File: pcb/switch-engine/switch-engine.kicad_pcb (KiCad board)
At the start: 10 copper layers, 124 x 112 mm, 368 parts, among them J1 CONN_PCIE_PWR_8PIN, J10 CORTEX_DEBUG_ETM, J11 SMPM, J12 CONN_01X03, J13 PMOD_HOST, J14 ARF6-08-S-D-A-K-TR, J15 ARF6-08-S-D-A-K-TR, J16 CONN_01X10, J17 ARF6-08-S-D-A-K-TR, J18 ARF6-08-S-D-A-K-TR, J19 CONN_01X10, J2 CONN_IBC_MGMT, J20 0826-1G1T-23-F, J21 ARF6-08-S-D-A-K-TR, J22 ARF6-08-S-D-A-K-TR, J23 CONN_01X10, J24 SMPM, J26 RJ45, J3 CONN_01X03, J4 CORTEX_DEBUG_ETM, J5 FAN_01, J6 FAN_01, J7 JUMPER_0402, J8 XILINX_JTAG, J9 PMOD_HOST, M1 SCREWHOLE, M2 SCREWHOLE, M3 SCREWHOLE, M4 SCREWHOLE, M5 LOGO, M6 LOGO, M7 LOGO, M8 960-27-23-D-AB-0, Q2 SSM6N58NU, SW1 SWITCH, SW2 SWITCH, U1 STM32L431-QFN48, U10 74LVC1T45, U11 74LVC1T45, U12 74LVC1T45, U13 MT25QU256ABA8E12-0AUT, U14 ECS-1612MV-250-CN, U15 SIT9121AI-2BF-XXS156.250000G, U17 AT24MAC402, U18 74LVC1T45, U19 74LVC1T45, U2 MYMGK1R812ERSR, U20 74LVC1T45, U21 74LVC1T45, U22 ECS-1612MV-250-CN, U23 KSZ9031RN, U24 ESD224DQAR, U25 SIT9121AI-2BF-XXS156.250000G, U26 ESD224DQAR, U27 SIT9121AI-2BF-XXS156.250000G, U28 ADP1740ACPZ-2.5-R7, U29 ADM3101E_QFN, U3 MYMGK1R812ERSR, U4 MYMGK00506ERSR, U5 MYMGK00504ERSR, U6 MYMGK00504ERSR, U7 ADP1740ACPZ-1.8-R7, U8 XCKU5P-2FFVB676I, U9 STM32H735-UFBGA176-25

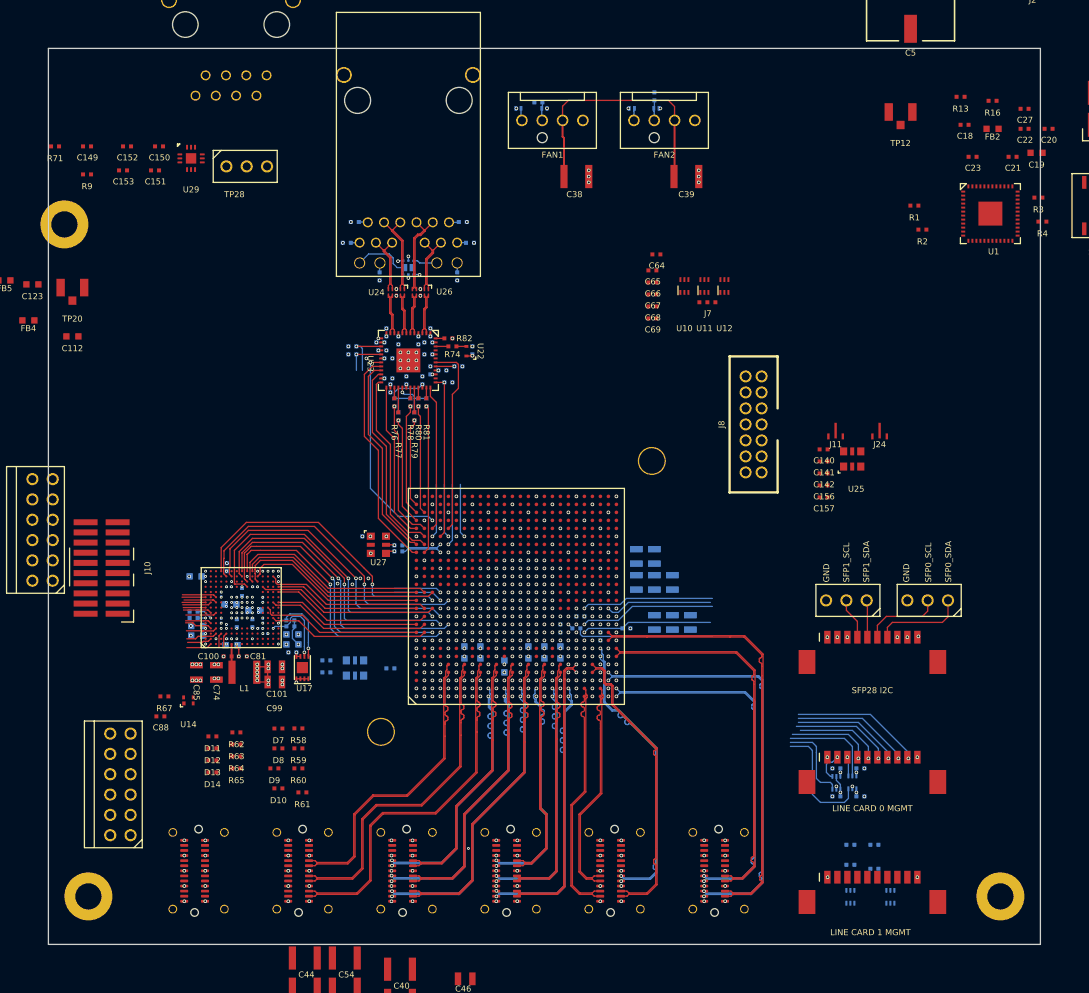
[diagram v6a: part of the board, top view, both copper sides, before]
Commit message: Continued routing southwest area
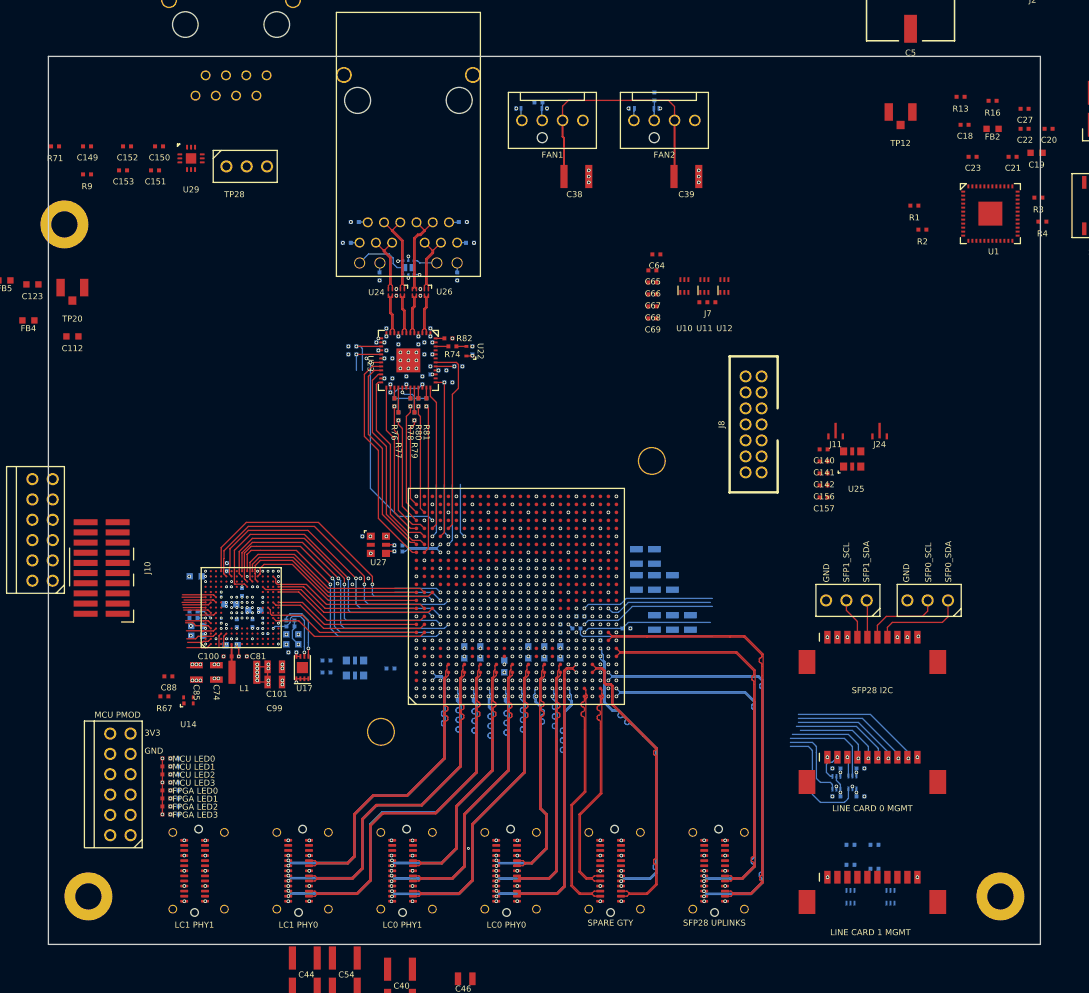
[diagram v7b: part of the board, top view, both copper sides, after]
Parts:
- R58, R59, R60, R61, R62, R63, R64, R65: moved to B.Cu
- moved R58 17.3 mm to (52.8, 122.8), turned to 180 degrees
- moved R59 16.7 mm to (52.8, 123.8), turned to 180 degrees
- moved R61 16.2 mm to (52.8, 125.8), turned to 180 degrees
- moved R60 16.2 mm to (52.8, 124.8), turned to 180 degrees
- moved D7 16.0 mm to (51.8, 122.8)
- moved D8 15.3 mm to (51.8, 123.8)
- moved D10 14.4 mm to (51.8, 125.8)
- moved D9 14.3 mm to (51.8, 124.8)
- moved R62 8.40 mm to (52.8, 118.8), turned to 180 degrees
- moved R63 8.22 mm to (52.8, 119.8), turned to 180 degrees
- moved R64 8.07 mm to (52.8, 120.8), turned to 180 degrees
- moved R65 7.95 mm to (52.8, 121.8), turned to 180 degrees
- moved D11 6.37 mm to (51.8, 118.8)
- moved D12 6.17 mm to (51.8, 119.8)
- moved D13 6.01 mm to (51.8, 120.8)
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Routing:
- net /Line card interfaces/LC1_PHY0_LANE0_RX_P: track 0.00 -> 45.0 mm, vias 1 -> 2
- net /Line card interfaces/LC1_PHY0_LANE0_RX_N: track 0.00 -> 45.0 mm, vias 1 -> 2
- net /Line card interfaces/LC1_PHY0_LANE1_RX_P: track 0.00 -> 41.3 mm, vias 1 -> 2
- net /Line card interfaces/LC1_PHY0_LANE1_RX_N: track 0.00 -> 41.3 mm, vias 1 -> 2
- net /Line card interfaces/LC1_PHY0_LANE2_RX_P: track 0.00 -> 40.1 mm, vias 1 -> 2
- net /Line card interfaces/LC1_PHY0_LANE2_RX_N: track 0.00 -> 40.1 mm, vias 1 -> 2
- net /GND: track 1063.4 -> 1056.4 mm, vias 397 -> 400
- net Net-(D9-A): vias 0 -> 1
- net Net-(D8-A): vias 0 -> 1
- net Net-(D7-A): vias 0 -> 1
- net Net-(D14-A): vias 0 -> 1
- net Net-(D13-A): vias 0 -> 1
- net Net-(D12-A): vias 0 -> 1
- net Net-(D11-A): vias 0 -> 1
- net Net-(D10-A): vias 0 -> 1
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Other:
- board size 124 x 112 mm -> 124 x 111 mm
- board text added: "3V3"
- board text added: "FPGA LED0"
- board text added: "FPGA LED1"
- board text added: "FPGA LED2"
- board text added: "FPGA LED3"
- board text added: "LC0 PHY0"
- board text added: "LC0 PHY1"
- board text added: "LC1 PHY0"
- board text added: "LC1 PHY1"
- board text added: "MCU LED0"
- board text added: "MCU LED1"
- board text added: "MCU LED2"
- board text added: "MCU LED3"
- board text added: "MCU PMOD"
- board text added: "SFP28 UPLINKS"
- board text added: "SPARE GTY"

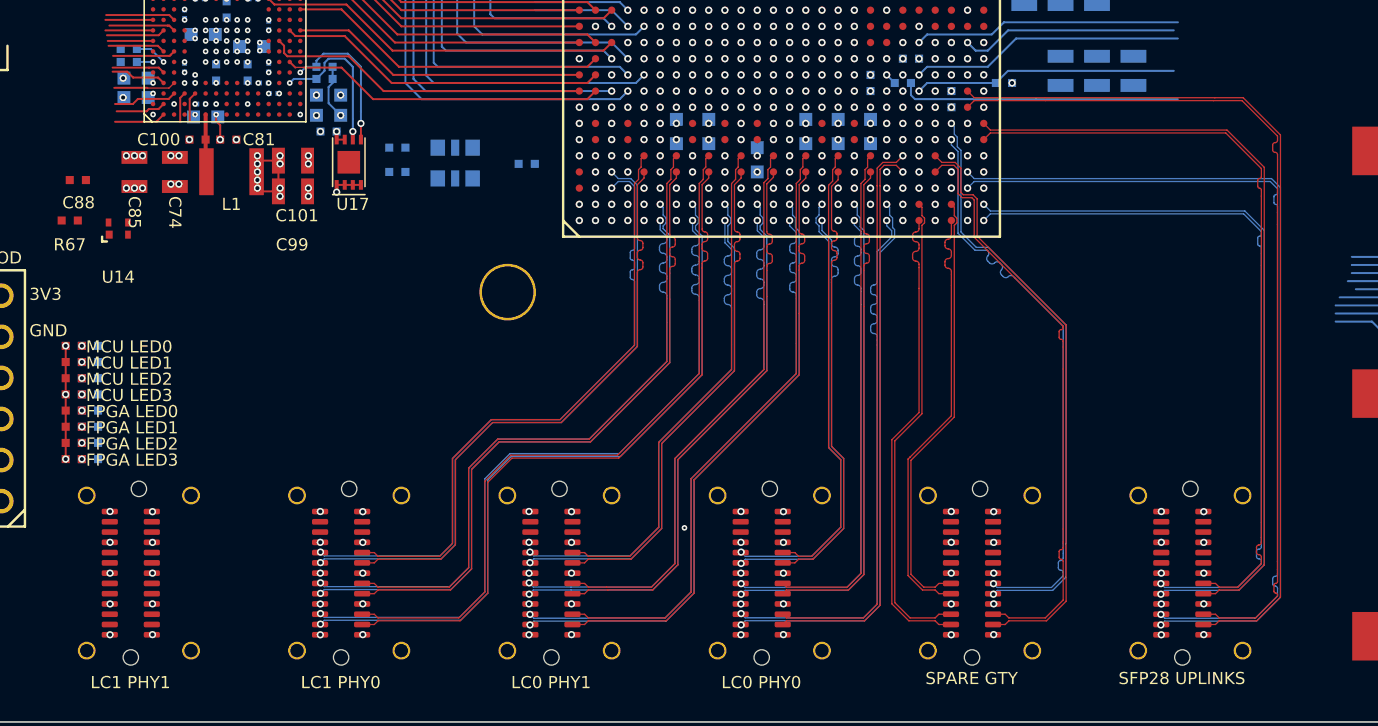
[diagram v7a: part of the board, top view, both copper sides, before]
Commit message: More tweaking to SERDES routing
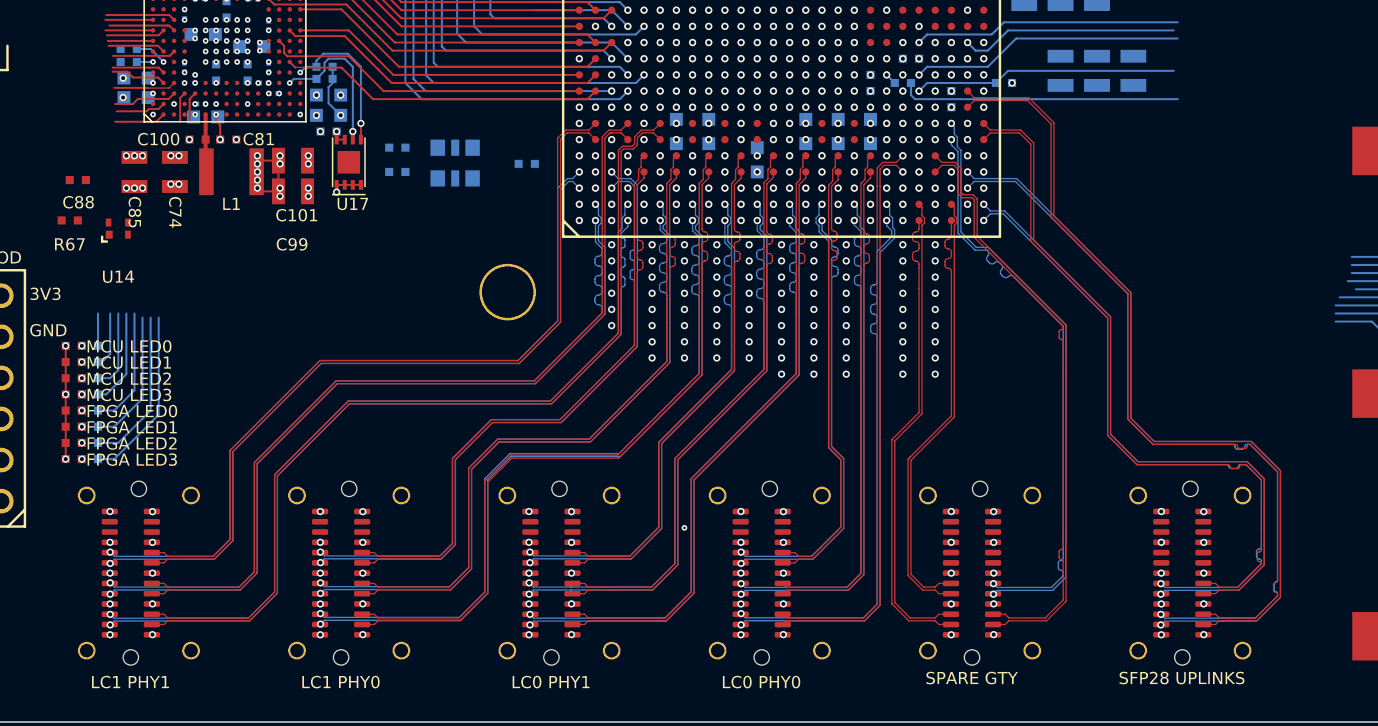
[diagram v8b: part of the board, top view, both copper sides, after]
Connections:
- U8 pad A3: /Line card interfaces/LC1_PHY1_LANE2_RX_N -> /Line card interfaces/LC1_PHY1_LANE2_RX_P
- U8 pad A4: /Line card interfaces/LC1_PHY1_LANE2_RX_P -> /Line card interfaces/LC1_PHY1_LANE2_RX_N
- U8 pad B6: /Line card interfaces/LC1_PHY1_LANE2_TX_N -> /Line card interfaces/LC1_PHY1_LANE2_TX_P
- U8 pad B7: /Line card interfaces/LC1_PHY1_LANE2_TX_P -> /Line card interfaces/LC1_PHY1_LANE2_TX_N
- U8 pad D1: /Line card interfaces/LC1_PHY1_LANE0_RX_N -> /Line card interfaces/LC1_PHY1_LANE0_RX_P
- U8 pad D2: /Line card interfaces/LC1_PHY1_LANE0_RX_P -> /Line card interfaces/LC1_PHY1_LANE0_RX_N
- U8 pad D6: /Line card interfaces/LC1_PHY1_LANE1_TX_N -> /Line card interfaces/LC1_PHY1_LANE1_TX_P
- U8 pad D7: /Line card interfaces/LC1_PHY1_LANE1_TX_P -> /Line card interfaces/LC1_PHY1_LANE1_TX_N
- U8 pad F6: /Line card interfaces/LC1_PHY1_LANE0_TX_N -> /Line card interfaces/LC1_PHY1_LANE0_TX_P
- U8 pad F7: /Line card interfaces/LC1_PHY1_LANE0_TX_P -> /Line card interfaces/LC1_PHY1_LANE0_TX_N
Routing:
- net /GND: track 1056.4 -> 1153.5 mm, vias 400 -> 483
- net /Line card interfaces/LC1_PHY1_LANE0_TX_P: track 0.00 -> 55.3 mm, vias 1 -> 0
- net /Line card interfaces/LC1_PHY1_LANE0_TX_N: track 0.00 -> 55.3 mm, vias 1 -> 0
- net /Line card interfaces/LC1_PHY1_LANE1_TX_N: track 0.00 -> 51.7 mm
- net /Line card interfaces/LC1_PHY1_LANE1_TX_P: track 0.00 -> 51.7 mm
- net /Line card interfaces/LC1_PHY1_LANE0_RX_N: track 0.00 -> 51.3 mm, vias 1 -> 2
- net /Line card interfaces/LC1_PHY1_LANE0_RX_P: track 0.00 -> 51.2 mm, vias 1 -> 2
- net /Line card interfaces/LC1_PHY1_LANE1_RX_P: track 0.00 -> 48.9 mm, vias 1 -> 2
- net /Line card interfaces/LC1_PHY1_LANE1_RX_N: track 0.00 -> 48.8 mm, vias 1 -> 2
- net /Line card interfaces/LC1_PHY1_LANE2_TX_N: track 0.00 -> 48.4 mm
- net /Line card interfaces/LC1_PHY1_LANE2_TX_P: track 0.00 -> 48.4 mm
- net /Line card interfaces/LC1_PHY1_LANE2_RX_P: track 0.00 -> 47.0 mm, vias 0 -> 2
- net /Line card interfaces/LC1_PHY1_LANE2_RX_N: track 0.00 -> 47.0 mm, vias 0 -> 2
- net /MCU/FPGA_LED_3: track 9.95 -> 20.8 mm
- net /MCU/FPGA_LED_2: track 9.85 -> 19.7 mm
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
